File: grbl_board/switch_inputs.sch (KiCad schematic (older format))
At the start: 22 parts, among them J10 DOOR, J11 PROBE, J12 INP, J13 LIM, U10 6N137, U11 6N137, U12 6N137, U13 6N137, U14 6N137, U15 6N137, U16 6N137, U17 6N137, U9 6N137

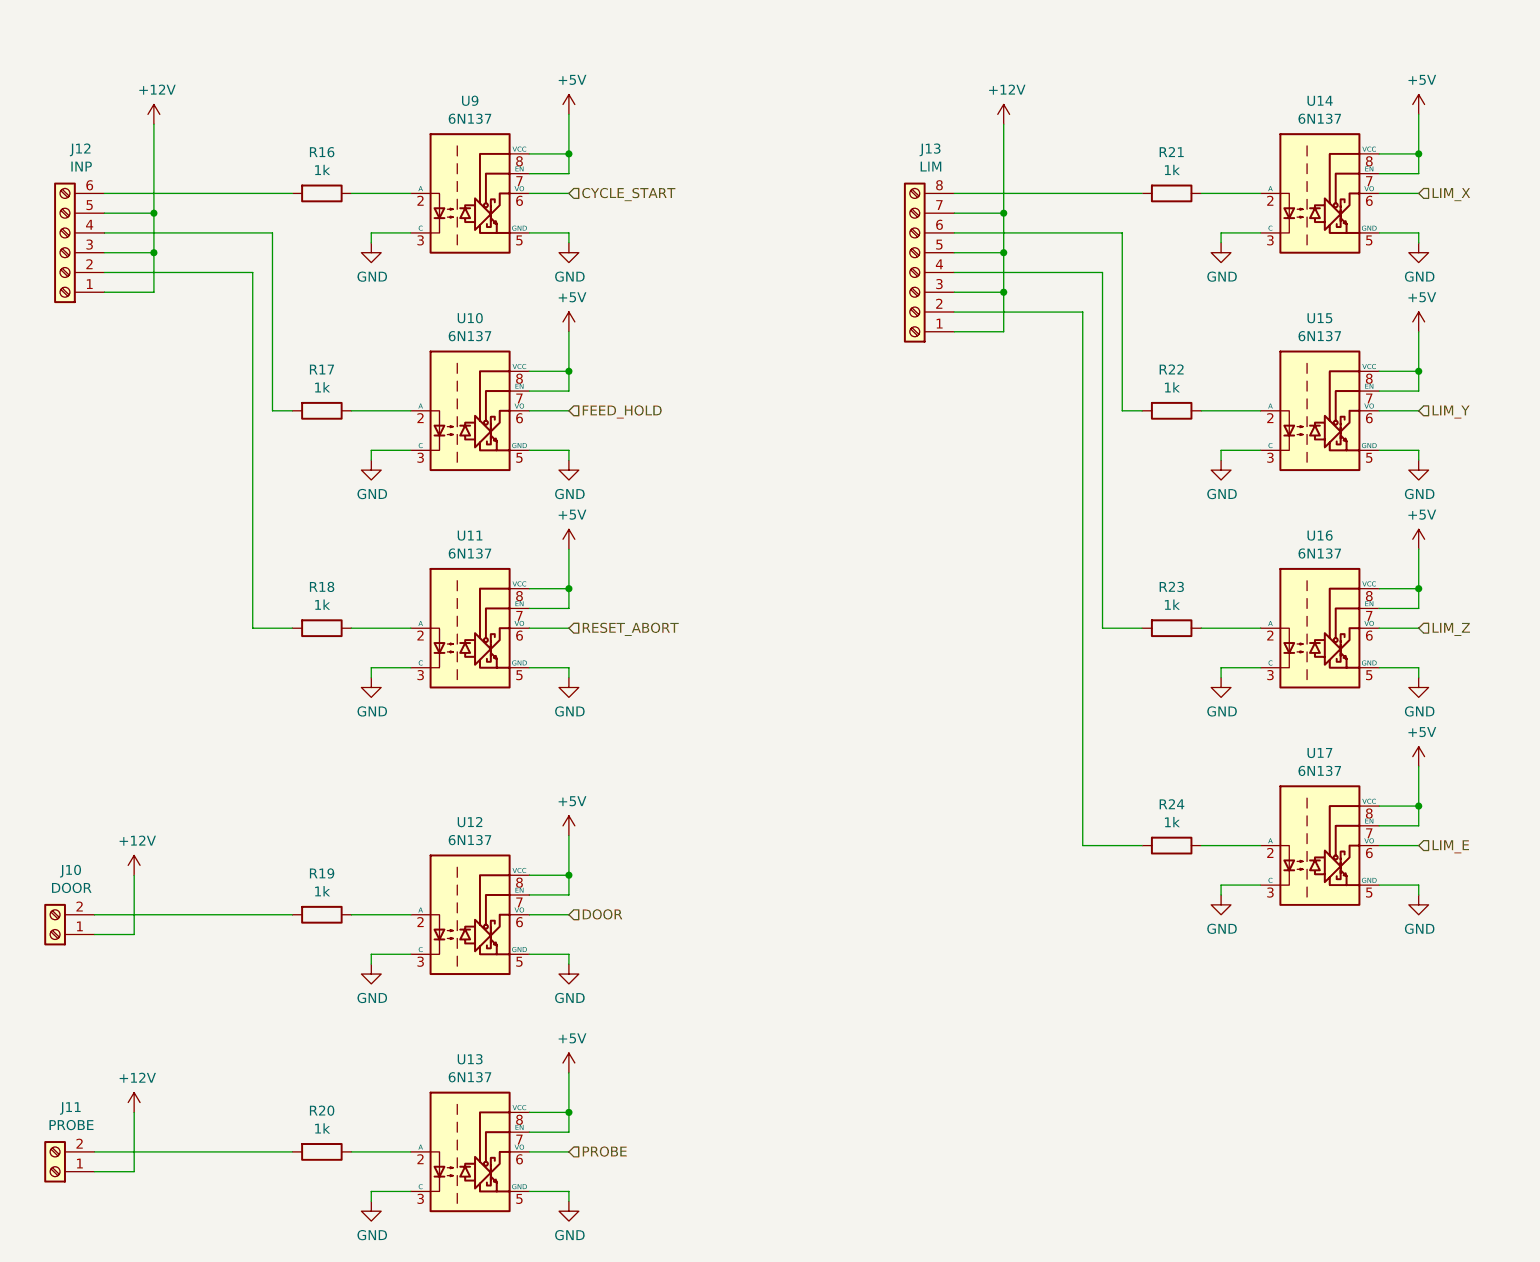
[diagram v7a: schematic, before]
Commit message: added some descriptions in the schematic and added gerber file
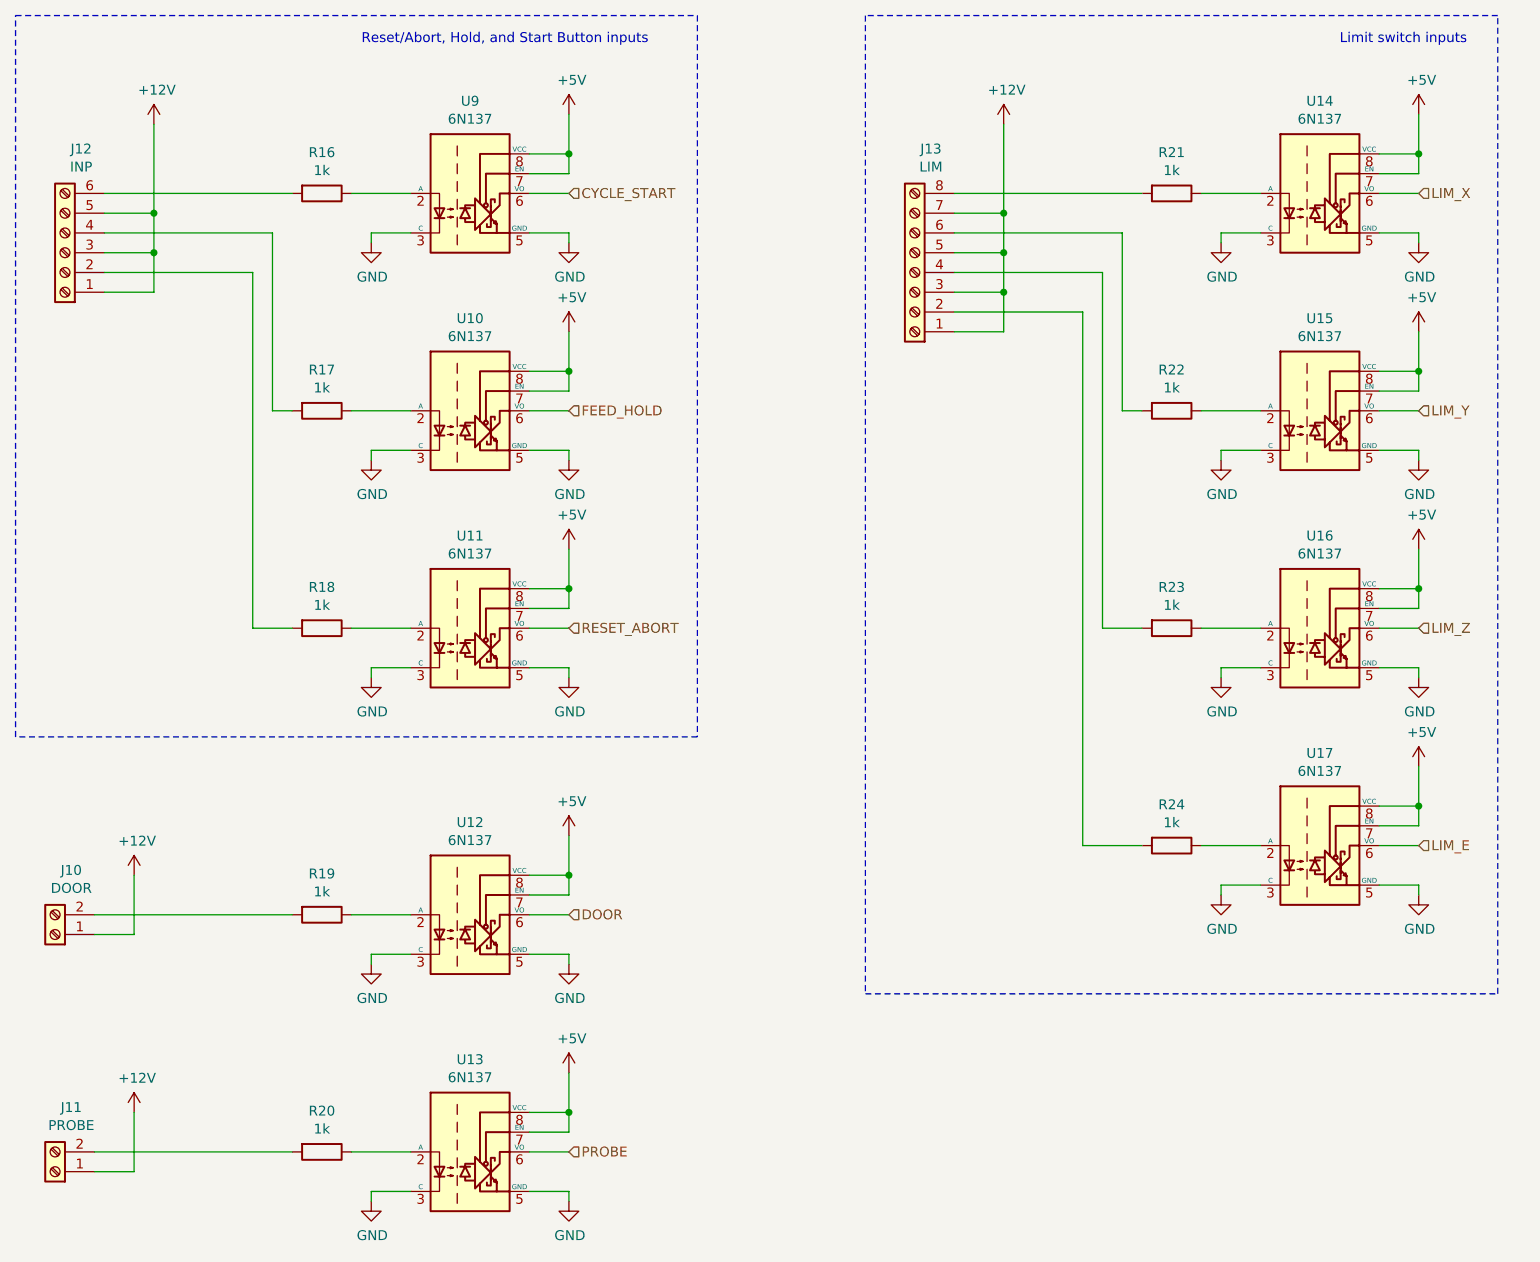
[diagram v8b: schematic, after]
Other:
- note added: "Limit switch inputs"
- note added: "Reset/Abort, Hold, and Start Button inputs\n"
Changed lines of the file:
@@
 Wire Wire Line
 	1800 7000 1600 7000
+Wire Notes Line
+	5500 1150 5500 6100
+Wire Notes Line
+	5500 6100 8700 6100
+Wire Notes Line
+	8700 6100 8700 1150
+Wire Notes Line
+	8700 1150 5500 1150
+Text Notes 7900 1300 0    50   ~ 0
+Limit switch inputs
+Wire Notes Line
+	4650 1150 4650 4800
+Wire Notes Line
+	4650 4800 1200 4800
+Wire Notes Line
+	1200 4800 1200 1150
+Wire Notes Line
+	1200 1150 4650 1150
+Text Notes 2950 1300 0    50   ~ 0
+Reset/Abort, Hold, and Start Button inputs\n
 $EndSCHEMATC
